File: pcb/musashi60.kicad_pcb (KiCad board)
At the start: 2 copper layers, 176.2 x 135.7 mm, 83 parts, among them J1 MJ-4PP-9, U1 ProMicro_r

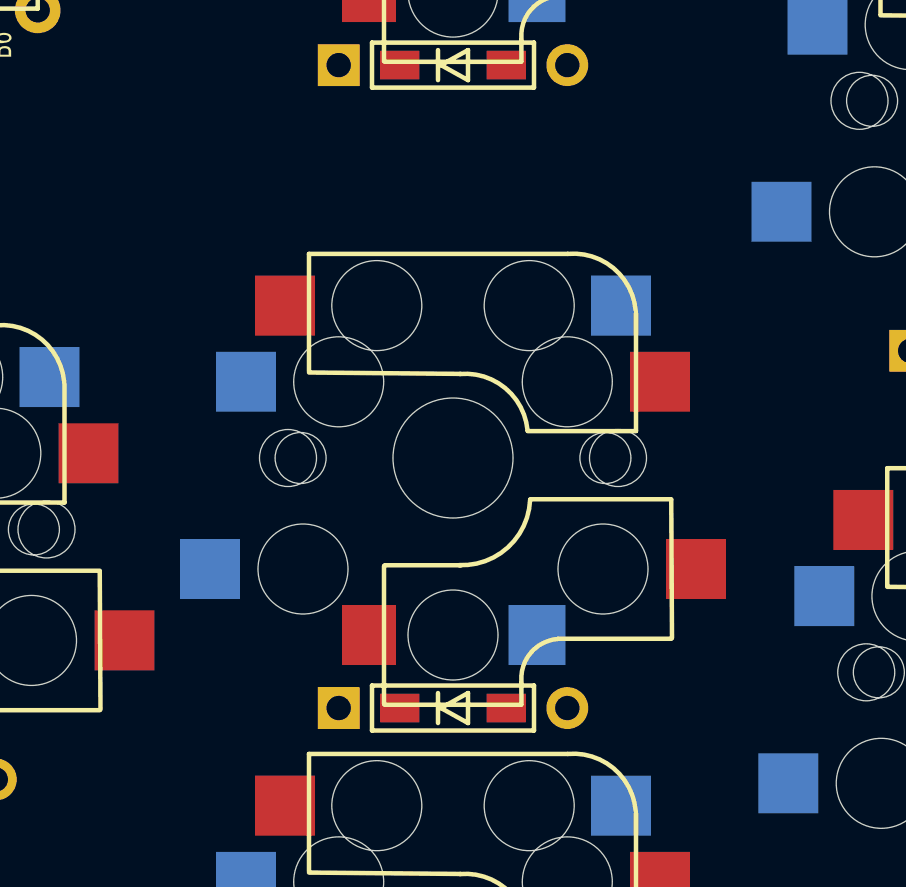
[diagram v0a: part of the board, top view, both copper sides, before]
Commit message: fix q and p layout
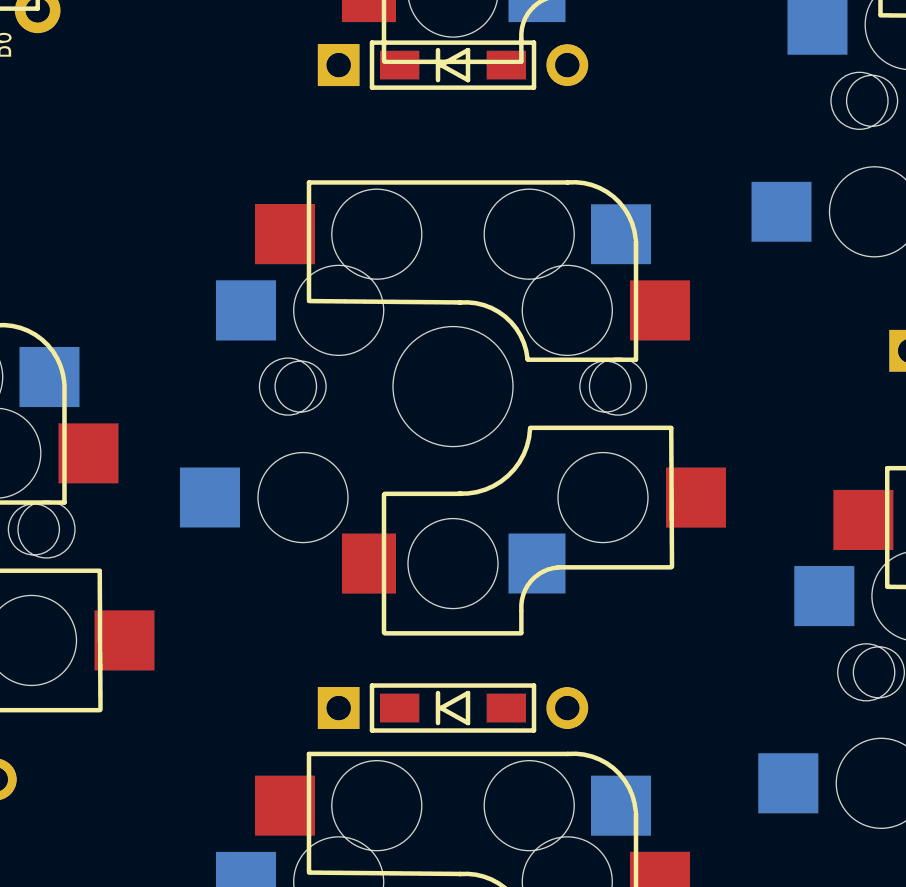
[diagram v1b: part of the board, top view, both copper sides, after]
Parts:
- moved SW_F2 2.38 mm to (61.9, 52.4)

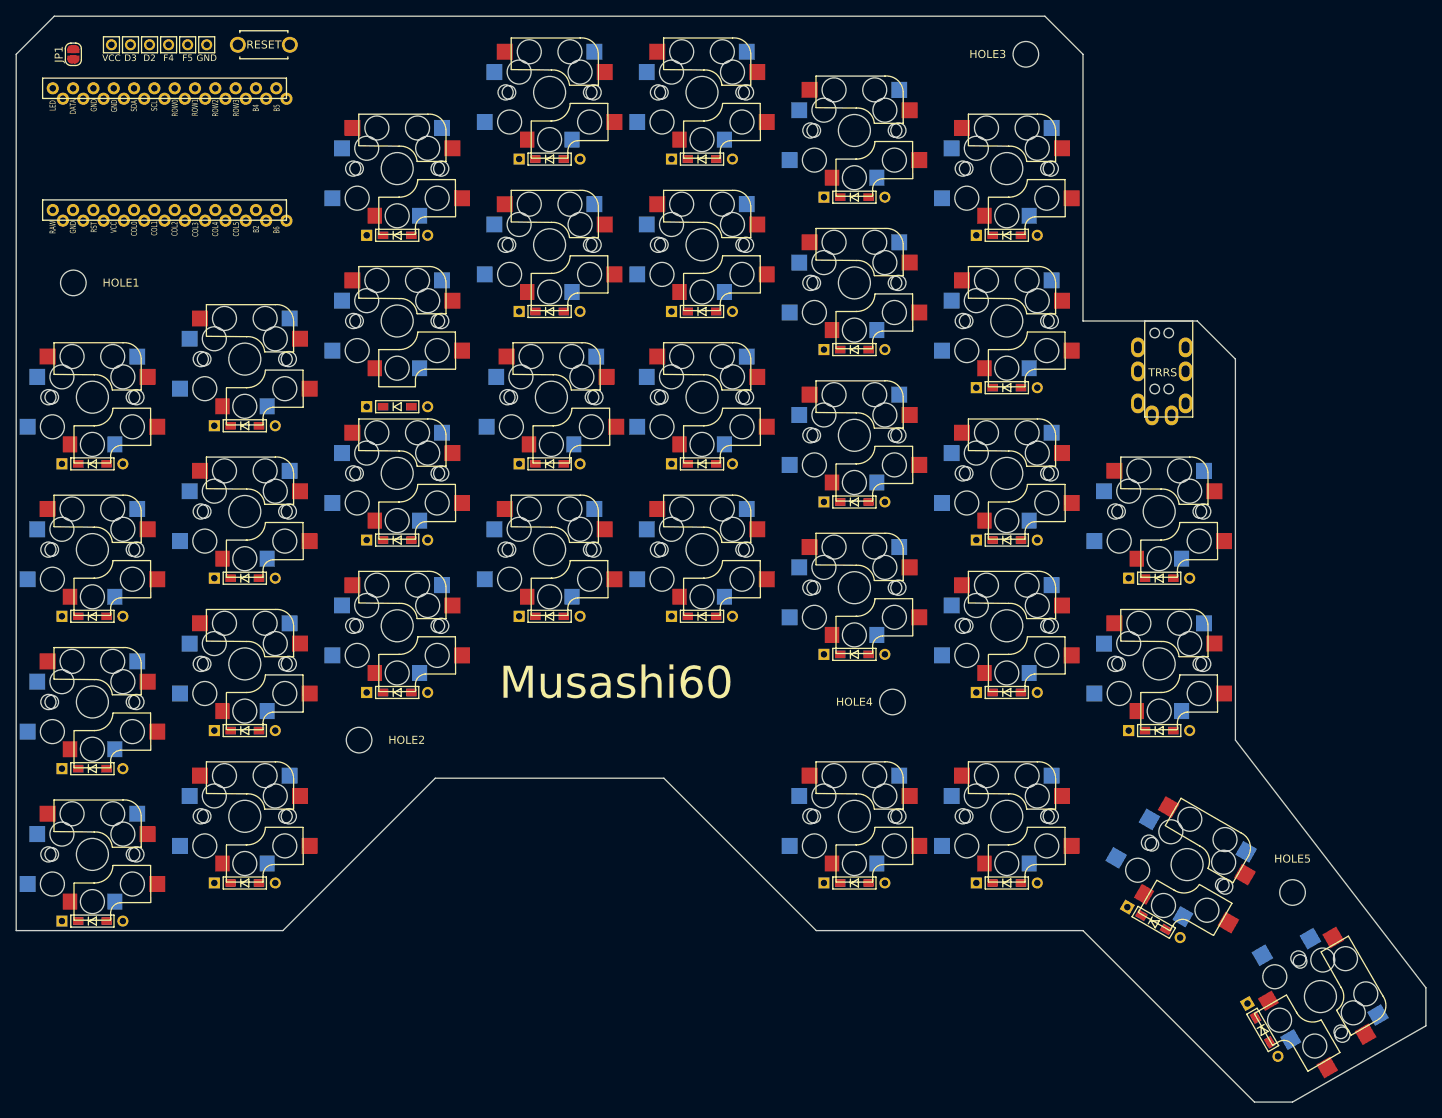
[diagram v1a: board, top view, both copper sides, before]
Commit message: remove mounting hole
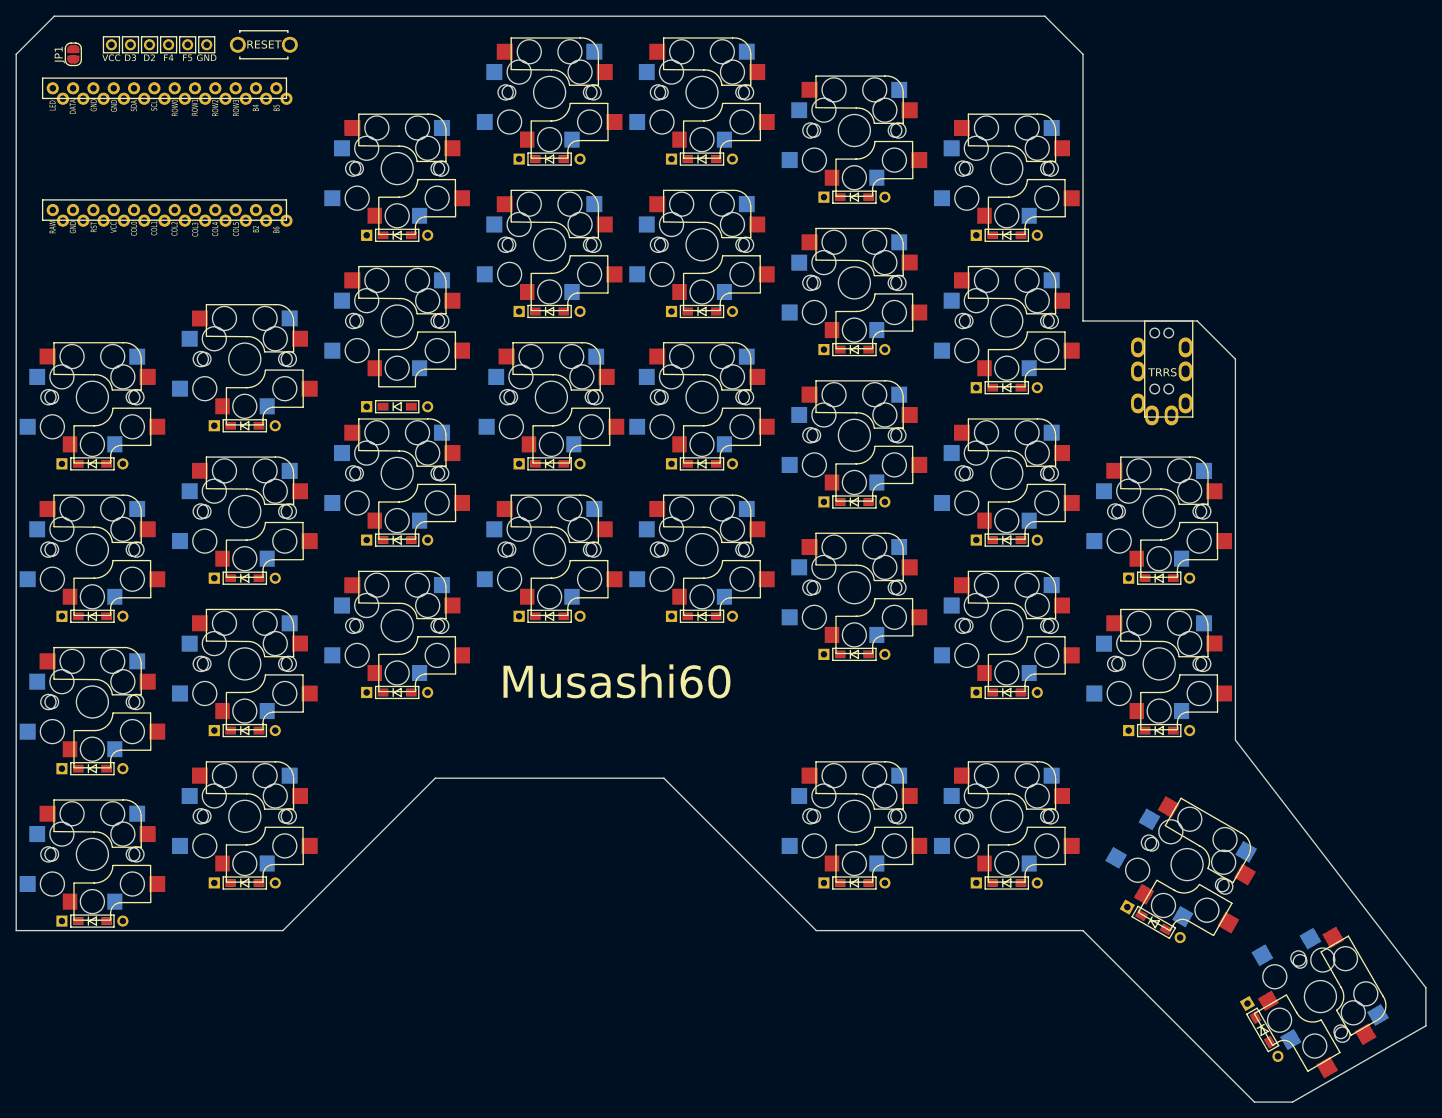
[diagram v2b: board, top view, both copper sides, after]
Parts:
- removed HOLE1, HOLE2, HOLE3, HOLE4, HOLE5: MountingHole_3.2mm_M3, MountingHole:MountingHole_3.2mm_M3
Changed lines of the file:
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@@
     (tracks 0)
     (zones 0)
-    (modules 83)
+    (modules 78)
     (nets 58)
   )
@@
     (add_net VCC)
   )
-  (module MountingHole:MountingHole_3.2mm_M3 (layer F.Cu)
-    (at 57.15024 104.77544)
-    (descr "Mounting Hole 3.2mm, no annular, M3")
-    (tags "mounting hole 3.2mm no annular m3")
-    (attr virtual)
-    (fp_text reference HOLE2 (at 5.95315 0.00044) (layer F.SilkS)
-      (effects (font (size 1 1) (thickness 0.15)))
-    )
-    (fp_text value MountingHole_3.2mm_M3 (at 0 4.2) (layer F.Fab)
-      (effects (font (size 1 1) (thickness 0.15)))
-    )
-    (fp_circle (center 0 0) (end 3.2 0) (layer Cmts.User) (width 0.15))
-    (fp_circle (center 0 0) (end 3.45 0) (layer F.CrtYd) (width 0.05))
-    (pad 1 np_thru_hole circle (at 0 0) (size 3.2 3.2) (drill 3.2) (layers *.Cu *.Mask))
-  )
-  (module MountingHole:MountingHole_3.2mm_M3 (layer F.Cu)
-    (at 123.825 100.0125)
-    (descr "Mounting Hole 3.2mm, no annular, M3")
-    (tags "mounting hole 3.2mm no annular m3")
-    (attr virtual)
-    (fp_text reference HOLE4 (at -4.762 0.00042) (layer F.SilkS)
-      (effects (font (size 1 1) (thickness 0.15)))
-    )
-    (fp_text value MountingHole_3.2mm_M3 (at 0 4.2) (layer F.Fab)
-      (effects (font (size 1 1) (thickness 0.15)))
-    )
-    (fp_circle (center 0 0) (end 3.2 0) (layer Cmts.User) (width 0.15))
-    (fp_circle (center 0 0) (end 3.45 0) (layer F.CrtYd) (width 0.05))
-    (fp_text user %R (at 0.3 0) (layer F.Fab)
-      (effects (font (size 1 1) (thickness 0.15)))
-    )
-    (pad 1 np_thru_hole circle (at 0 0) (size 3.2 3.2) (drill 3.2) (layers *.Cu *.Mask))
-  )
-  (module MountingHole:MountingHole_3.2mm_M3 (layer F.Cu)
-    (at 173.83125 123.825)
-    (descr "Mounting Hole 3.2mm, no annular, M3")
-    (tags "mounting hole 3.2mm no annular m3")
-    (attr virtual)
-    (fp_text reference HOLE5 (at 0 -4.2) (layer F.SilkS)
-      (effects (font (size 1 1) (thickness 0.15)))
-    )
-    (fp_text value MountingHole_3.2mm_M3 (at 0 4.2) (layer F.Fab)
-      (effects (font (size 1 1) (thickness 0.15)))
-    )
-    (fp_circle (center 0 0) (end 3.2 0) (layer Cmts.User) (width 0.15))
-    (fp_circle (center 0 0) (end 3.45 0) (layer F.CrtYd) (width 0.05))
-    (fp_text user %R (at 0.3 0) (layer F.Fab)
-      (effects (font (size 1 1) (thickness 0.15)))
-    )
-    (pad 1 np_thru_hole circle (at 0 0) (size 3.2 3.2) (drill 3.2) (layers *.Cu *.Mask))
-  )
-  (module MountingHole:MountingHole_3.2mm_M3 (layer F.Cu)
-    (at 140.49434 19.05008)
-    (descr "Mounting Hole 3.2mm, no annular, M3")
-    (tags "mounting hole 3.2mm no annular m3")
-    (attr virtual)
-    (fp_text reference HOLE3 (at -4.76252 0) (layer F.SilkS)
-      (effects (font (size 1 1) (thickness 0.15)))
-    )
-    (fp_text value MountingHole_3.2mm_M3 (at 0 4.2) (layer F.Fab)
-      (effects (font (size 1 1) (thickness 0.15)))
-    )
-    (fp_circle (center 0 0) (end 3.2 0) (layer Cmts.User) (width 0.15))
-    (fp_circle (center 0 0) (end 3.45 0) (layer F.CrtYd) (width 0.05))
-    (fp_text user %R (at 0.3 0) (layer F.Fab)
-      (effects (font (size 1 1) (thickness 0.15)))
-    )
-    (pad 1 np_thru_hole circle (at 0 0) (size 3.2 3.2) (drill 3.2) (layers *.Cu *.Mask))
-  )
-  (module MountingHole:MountingHole_3.2mm_M3 (layer F.Cu)
-    (at 21.43134 47.6252)
-    (descr "Mounting Hole 3.2mm, no annular, M3")
-    (tags "mounting hole 3.2mm no annular m3")
-    (attr virtual)
-    (fp_text reference HOLE1 (at 5.95315 0) (layer F.SilkS)
-      (effects (font (size 1 1) (thickness 0.15)))
-    )
-    (fp_text value MountingHole_3.2mm_M3 (at 0 4.2) (layer F.Fab)
-      (effects (font (size 1 1) (thickness 0.15)))
-    )
-    (fp_circle (center 0 0) (end 3.2 0) (layer Cmts.User) (width 0.15))
-    (fp_circle (center 0 0) (end 3.45 0) (layer F.CrtYd) (width 0.05))
-    (fp_text user %R (at 0.3 0) (layer F.Fab)
-      (effects (font (size 1 1) (thickness 0.15)))
-    )
-    (pad 1 np_thru_hole circle (at 0 0) (size 3.2 3.2) (drill 3.2) (layers *.Cu *.Mask))
-  )
   (module foostan:MJ-4PP-9 (layer F.Cu)

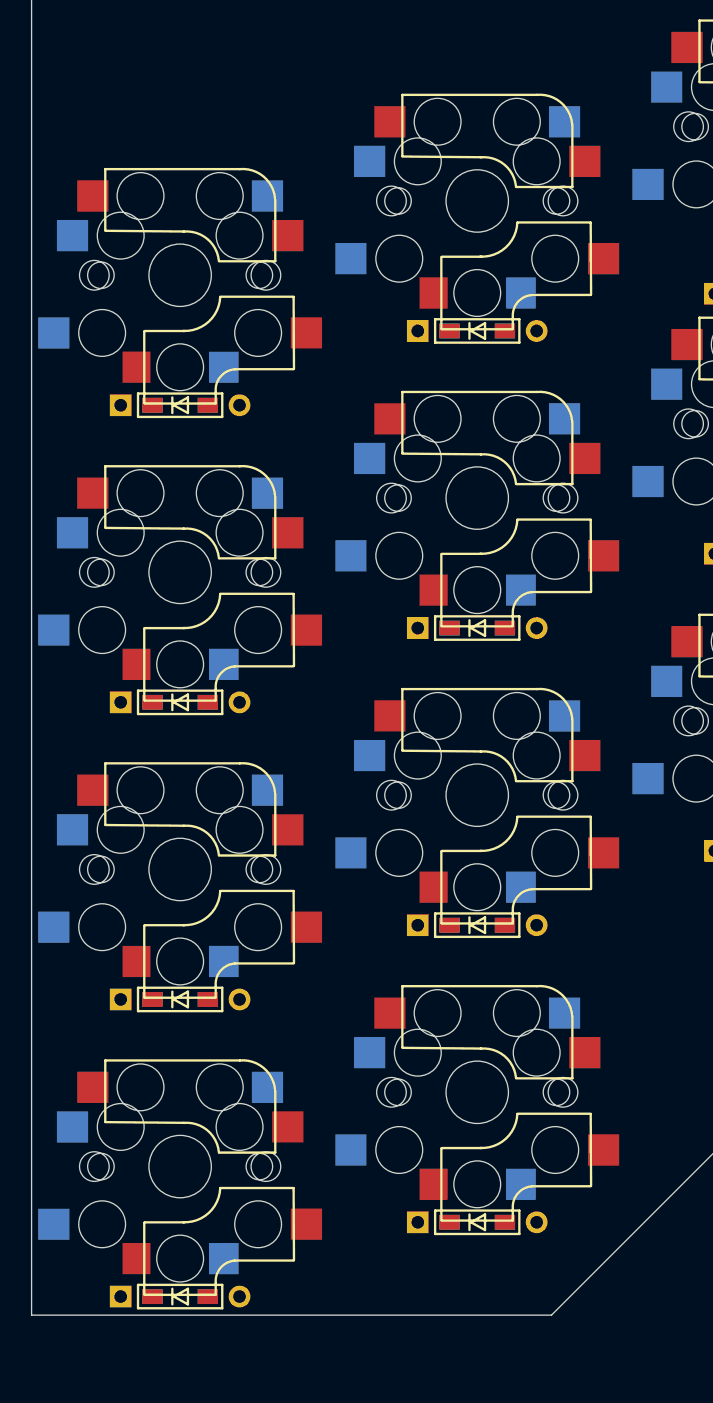
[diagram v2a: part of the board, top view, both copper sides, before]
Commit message: fix colG and colH
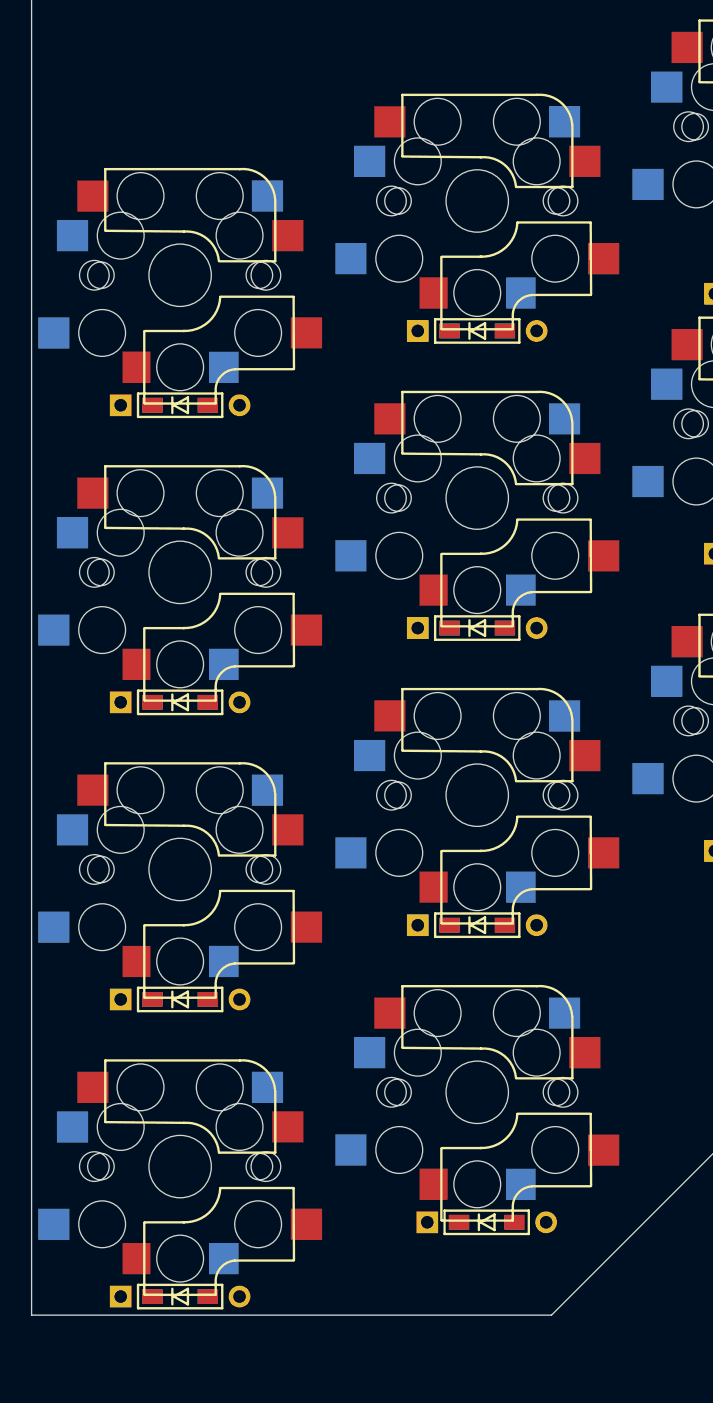
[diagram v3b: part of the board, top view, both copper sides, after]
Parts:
- moved D_G5 20.2 mm to (43.5, 122.6)
- moved SW_G2 19.6 mm to (42.9, 57.2)
- moved D_G2 19.6 mm to (42.9, 65.5)
- moved SW_G3 19.6 mm to (42.9, 76.2)
- moved D_G3 19.6 mm to (42.9, 84.5)
- moved SW_G4 19.6 mm to (42.9, 95.3)
- moved D_G4 19.6 mm to (42.9, 103.6)
- moved SW_G5 19.6 mm to (42.9, 114.3)
- moved D_H5 19.6 mm to (23.8, 127.4)
- moved SW_H5 19.6 mm to (23.8, 119.1)
- moved D_H4 19.6 mm to (23.8, 108.3)
- moved SW_H4 19.6 mm to (23.8, 100.0)
- moved D_H3 19.6 mm to (23.8, 89.3)
- moved SW_H3 19.6 mm to (23.8, 81.0)
- moved D_H2 19.6 mm to (23.8, 70.2)
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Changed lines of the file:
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@@
   )
   (module foostan:D3_TH_SMD (layer F.Cu)
-    (at 23.8125 70.246875)
+    (at 42.86268 65.48465)
     (descr "Resitance 3 pas")
     (tags R)
@@
   )
   (module foostan:D3_TH_SMD (layer F.Cu)
-    (at 23.8125 89.296875)
+    (at 42.86268 84.53473)
     (descr "Resitance 3 pas")
     (tags R)
@@
   )
   (module foostan:D3_TH_SMD (layer F.Cu)
-    (at 23.8125 108.346875)
+    (at 42.86268 103.58481)
     (descr "Resitance 3 pas")
     (tags R)
@@
   )
   (module foostan:D3_TH_SMD (layer F.Cu)
-    (at 23.8125 127.396875)
+    (at 43.46894 122.63489)
     (descr "Resitance 3 pas")
     (tags R)
@@
   )
   (module foostan:D3_TH_SMD (layer F.Cu)
-    (at 42.8625 65.484375)
+    (at 23.8126 70.24717)
     (descr "Resitance 3 pas")
     (tags R)
@@
   )
   (module foostan:D3_TH_SMD (layer F.Cu)
-    (at 42.8625 84.534375)
+    (at 23.8126 89.29725)
     (descr "Resitance 3 pas")
     (tags R)
@@
   )
   (module foostan:D3_TH_SMD (layer F.Cu)
-    (at 42.8625 103.584375)
+    (at 23.8126 108.34733)
     (descr "Resitance 3 pas")
     (tags R)
@@
   )
   (module foostan:D3_TH_SMD (layer F.Cu)
-    (at 42.8625 122.634375)
+    (at 23.8126 127.39741)
     (descr "Resitance 3 pas")
     (tags R)
@@
   )
   (module foostan:CherryMX_Choc_Hotswap (layer F.Cu)
-    (at 23.8125 61.9125)
+    (at 42.86268 57.15024)
     (fp_text reference SW_G2 (at 7 8.1) (layer F.SilkS) hide
       (effects (font (size 1 1) (thickness 0.15)))
@@
   )
   (module foostan:CherryMX_Choc_Hotswap (layer F.Cu)
-    (at 23.8125 80.9625)
+    (at 42.86268 76.20032)
     (fp_text reference SW_G3 (at 7 8.1) (layer F.SilkS) hide
       (effects (font (size 1 1) (thickness 0.15)))
@@
   )
   (module foostan:CherryMX_Choc_Hotswap (layer F.Cu)
-    (at 23.8125 100.0125)
+    (at 42.86268 95.2504)
     (fp_text reference SW_G4 (at 7 8.1) (layer F.SilkS) hide
       (effects (font (size 1 1) (thickness 0.15)))
@@
   )
   (module foostan:CherryMX_Choc_Hotswap (layer F.Cu)
-    (at 23.8125 119.0625)
+    (at 42.86268 114.30048)
     (fp_text reference SW_G5 (at 7 8.1) (layer F.SilkS) hide
       (effects (font (size 1 1) (thickness 0.15)))
@@
   )
   (module foostan:CherryMX_Choc_Hotswap (layer F.Cu)
-    (at 42.8625 57.15)
+    (at 23.8126 61.91276)
     (fp_text reference SW_H2 (at 7 8.1) (layer F.SilkS) hide
       (effects (font (size 1 1) (thickness 0.15)))
@@
   )
   (module foostan:CherryMX_Choc_Hotswap (layer F.Cu)
-    (at 42.8625 76.2)
+    (at 23.8126 80.96284)
     (fp_text reference SW_H3 (at 7 8.1) (layer F.SilkS) hide
       (effects (font (size 1 1) (thickness 0.15)))
@@
   )
   (module foostan:CherryMX_Choc_Hotswap (layer F.Cu)
-    (at 42.8625 95.25)
+    (at 23.8126 100.01292)
     (fp_text reference SW_H4 (at 7 8.1) (layer F.SilkS) hide
       (effects (font (size 1 1) (thickness 0.15)))
@@
   )
   (module foostan:CherryMX_Choc_Hotswap (layer F.Cu)
-    (at 42.8625 114.3)
+    (at 23.8126 119.063)
     (fp_text reference SW_H5 (at 7 8.1) (layer F.SilkS) hide
       (effects (font (size 1 1) (thickness 0.15)))

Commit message: update pcb
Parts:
- added JP_RIGHT1: Jumper, Jumper:SolderJumper-2_P1.3mm_Open_RoundedPad1.0x1.5mm, B.Cu at (19.1, 19.1)
- moved SW_RST1 35.5 mm to (24.1, 46.4)
- moved SW_D5 5.32 mm to (116.7, 109.5)
- moved J1 3.57 mm to (154.8, 52.4)
- moved SW_A5 3.49 mm to (173.8, 136.9)
- moved SW_B5 3.49 mm to (157.2, 120.3)
- moved SW_C5 1.99 mm to (137.9, 112.3), turned to 345 degrees
- turned JP_LEFT1 to 270 degrees
- renumbered D2 to H_D2, D3 to H_D3, F4 to H_F4, F5 to H_F5, GND to H_GND1, VCC to H_VCC1, JP1 to JP_LEFT1
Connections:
- JP_LEFT1 pad 1: GND -> VCC
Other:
- board size 176.2 x 135.7 mm -> 175 x 135.7 mm
